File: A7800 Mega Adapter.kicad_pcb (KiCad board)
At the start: 2 copper layers, 30.5 x 31.8 mm, 8 parts, among them J1 Atari 7800, J2 Mega Drive, Q1 2N3906, Q2 2N3906

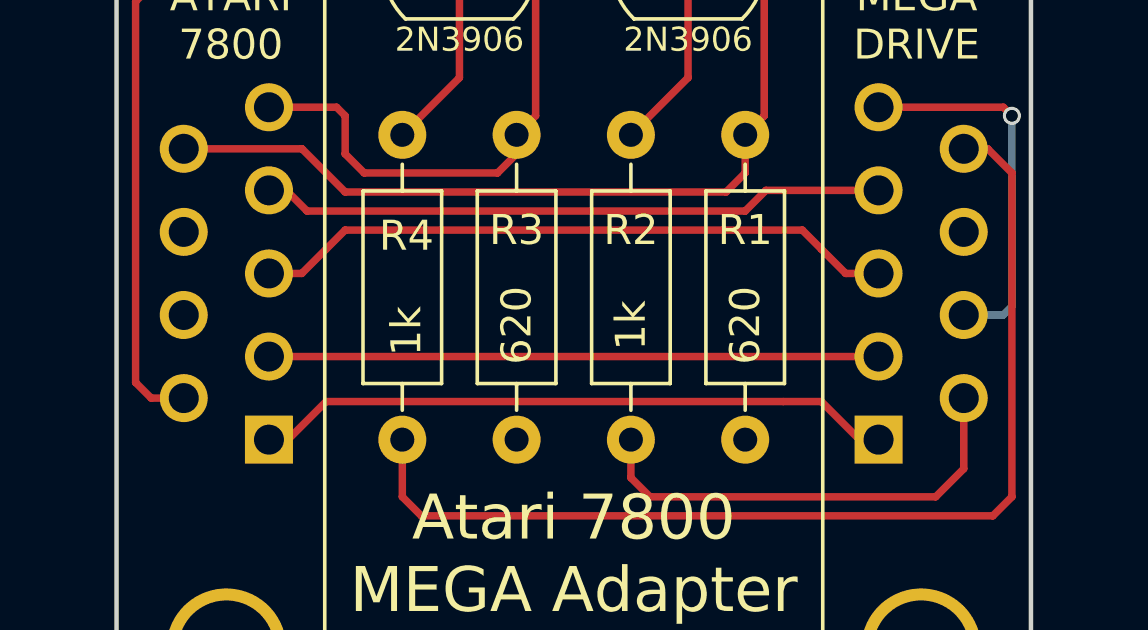
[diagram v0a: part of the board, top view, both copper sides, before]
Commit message: Fixed VCC wire
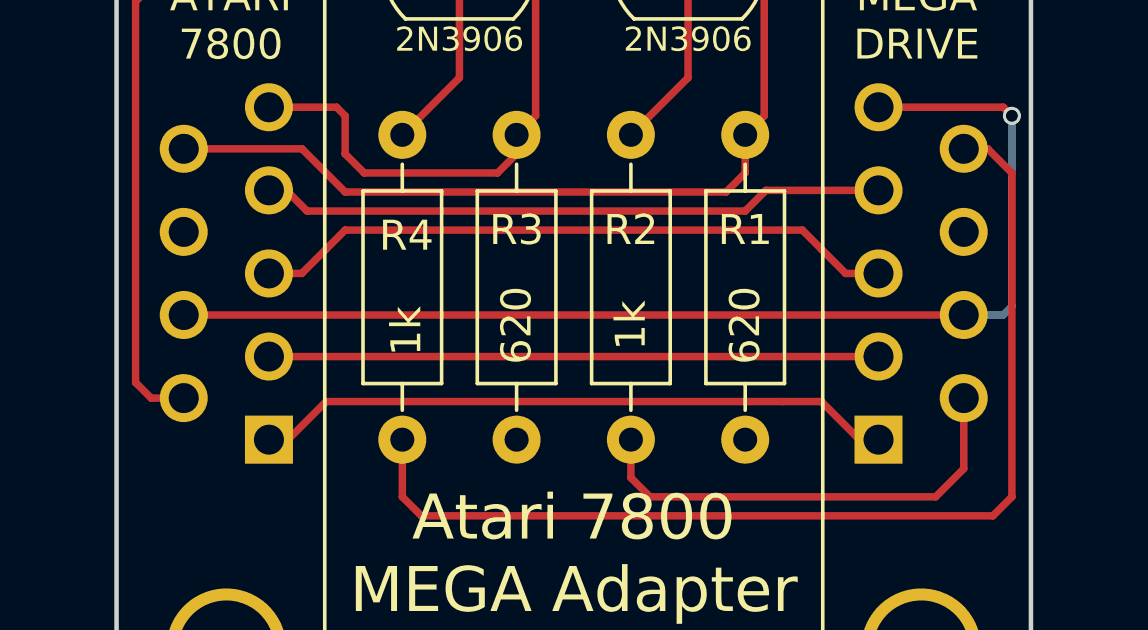
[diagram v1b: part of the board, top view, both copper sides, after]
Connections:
- J1 pad 7: (no net) -> VCC
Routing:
- net VCC: track 12.6 -> 38.6 mm
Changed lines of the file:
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@@
 (kicad_pcb (version 4) (host pcbnew 4.0.7)
   (general
-    (links 18)
+    (links 19)
     (no_connects 0)
-    (area 83.185 53.34 163.195001 100.330001)
+    (area 116.129999 58.979999 146.760001 90.880001)
     (thickness 1.6)
     (drawings 14)
-    (tracks 68)
+    (tracks 69)
     (zones 0)
     (modules 8)
@@
     (pad 6 thru_hole circle (at -1.385 2.84 270) (size 1.6 1.6) (drill 1) (layers *.Cu *.Mask)
       (net 7 FIRE))
-    (pad 7 thru_hole circle (at -4.155 2.84 270) (size 1.6 1.6) (drill 1) (layers *.Cu *.Mask))
+    (pad 7 thru_hole circle (at -4.155 2.84 270) (size 1.6 1.6) (drill 1) (layers *.Cu *.Mask)
+      (net 1 VCC))
     (pad 8 thru_hole circle (at -6.925 2.84 270) (size 1.6 1.6) (drill 1) (layers *.Cu *.Mask)
       (net 2 GND))
@@
     (effects (font (size 1.5 1.5) (thickness 0.15)))
   )
+  (segment (start 118.445 76.49) (end 144.445 76.49) (width 0.25) (layer F.Cu) (net 1))
   (segment (start 141.605 69.565) (end 145.765 69.565) (width 0.25) (layer F.Cu) (net 1))
   (segment (start 145.76 76.49) (end 144.445 76.49) (width 0.25) (layer B.Cu) (net 1))
